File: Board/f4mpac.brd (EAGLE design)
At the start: 60.3 x 83.2 mm, 52 parts, among them CN1 DIP40 MB CONN, IC1 YM2413, IC10 27C512AL, IC2 74LS30D, IC3 74LS04D, IC4 LM4558N, IC5 Z80, IC6 74LS30D, IC7 74LS02D, IC8 74LS74D, IC9 74LS125D

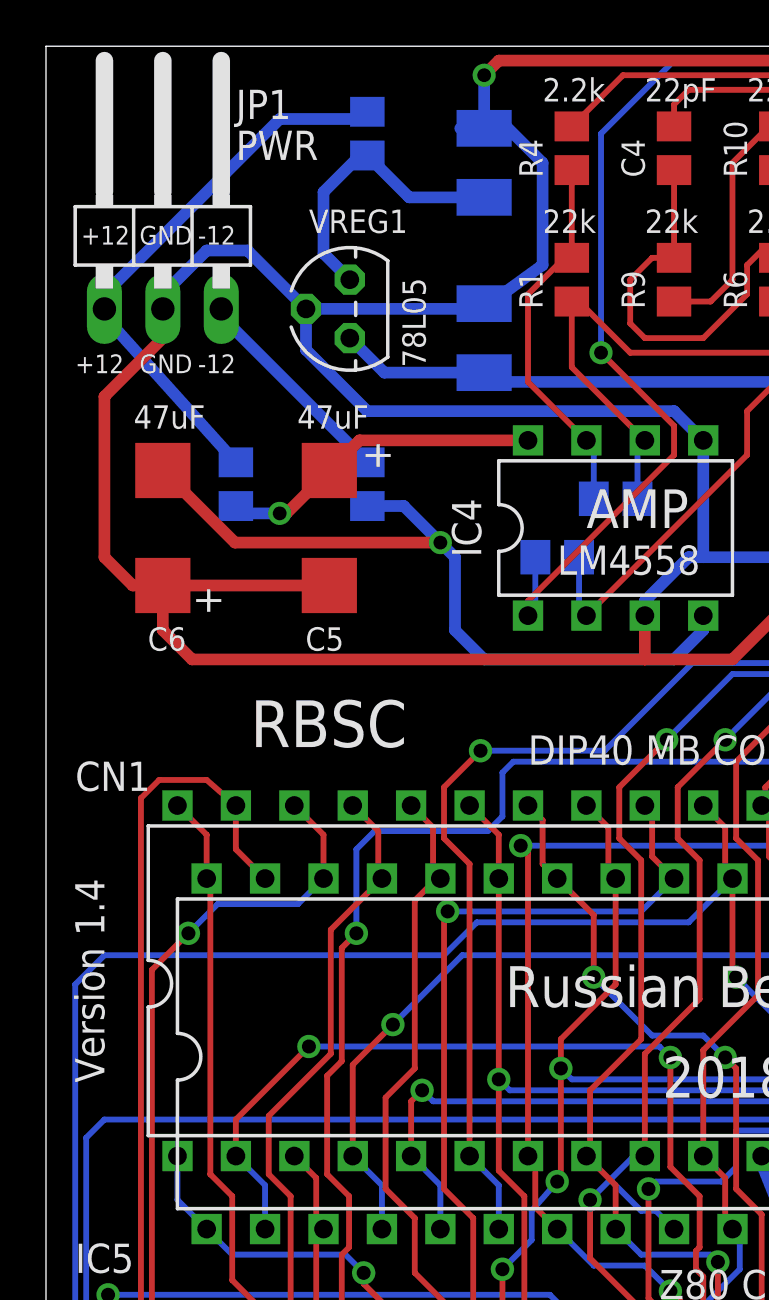
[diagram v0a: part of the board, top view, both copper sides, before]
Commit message: Updated 14.05.2025
Updated the board to version 1.5. Corrected R4, C14 and C16 values. Updated readme file.
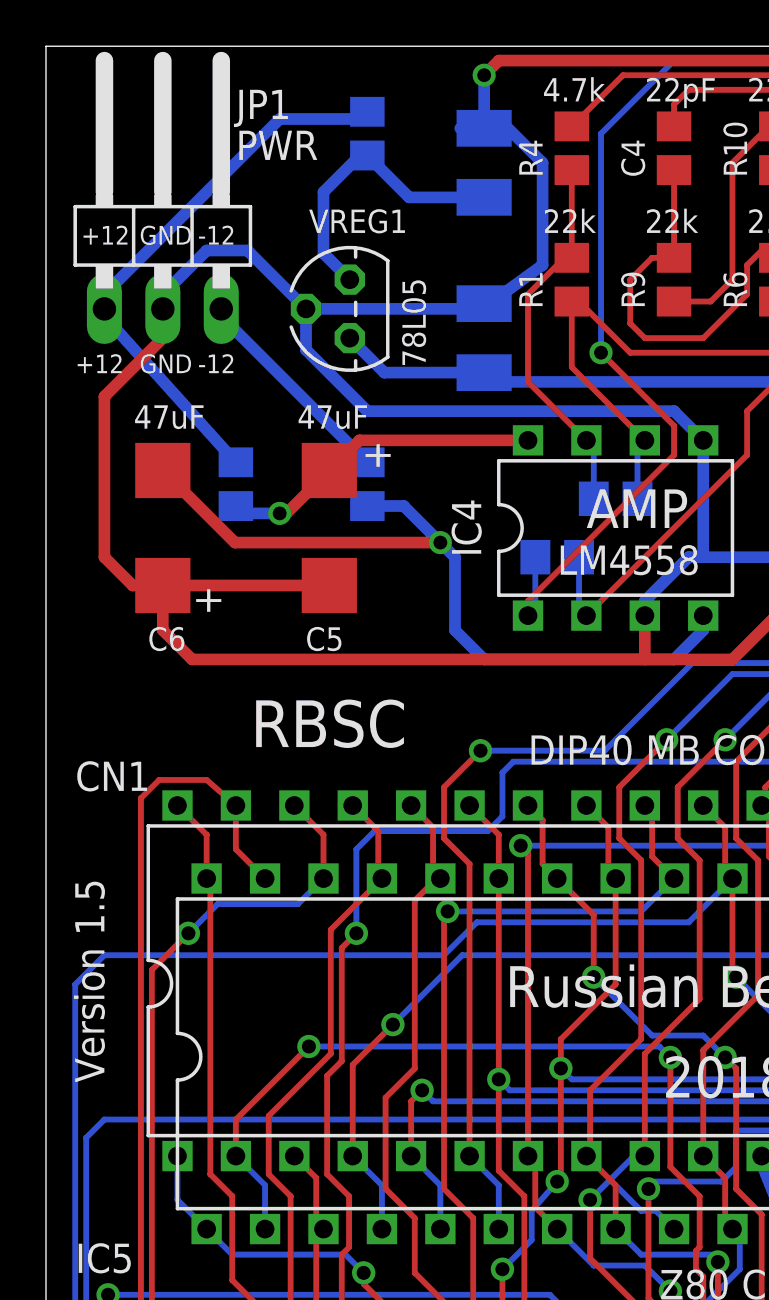
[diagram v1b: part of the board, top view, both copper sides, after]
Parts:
- C14, C16: value 1nF -> 470pF
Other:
- board text added: "470pF"
- board text added: "Version 1.5"
- board text removed: "1nF"
- board text removed: "Version 1.4"
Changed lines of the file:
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@@
 <text x="21.59" y="74.422" size="1.016" layer="25" font="vector">22k</text>
 <text x="34.925" y="74.422" size="1.016" layer="25" font="vector">2.2k</text>
-<text x="21.59" y="80.137" size="1.016" layer="25" font="vector">2.2k</text>
+<text x="21.59" y="80.137" size="1.016" layer="25" font="vector">4.7k</text>
 <text x="43.815" y="74.422" size="1.016" layer="25" font="vector">2.2k</text>
 <text x="26.035" y="74.422" size="1.016" layer="25" font="vector">22k</text>
@@
 <wire x1="20.32" y1="3.81" x2="40.64" y2="3.81" width="0.254" layer="25"/>
 <wire x1="40.64" y1="3.81" x2="40.64" y2="25.4" width="0.254" layer="25"/>
-<text x="17.145" y="61.595" size="1.016" layer="26" font="vector" rot="MR180">C14</text>
-<text x="17.145" y="60.325" size="1.016" layer="26" font="vector" rot="MR180">1nF</text>
+<text x="17.145" y="60.96" size="1.016" layer="26" font="vector" rot="MR180">C14</text>
+<text x="17.145" y="62.23" size="1.016" layer="26" font="vector" rot="MR180">470pF</text>
 <text x="11.43" y="74.422" size="1.016" layer="25" font="vector">VREG1</text>
 <text x="16.51" y="68.58" size="1.016" layer="25" font="vector" rot="R90">78L05</text>
@@
 <wire x1="40.64" y1="25.4" x2="20.32" y2="25.4" width="0.254" layer="25"/>
 <wire x1="20.32" y1="25.4" x2="20.32" y2="3.81" width="0.254" layer="25"/>
-<text x="26.797" y="71.12" size="1.27" layer="26" font="vector" rot="MR180">Version 1.4</text>
-<text x="1.27" y="46.355" size="1.27" layer="25" font="vector" rot="R270">Version 1.4</text>
+<text x="26.797" y="71.12" size="1.27" layer="26" font="vector" rot="MR180">Version 1.5</text>
+<text x="1.27" y="46.355" size="1.27" layer="25" font="vector" rot="R270">Version 1.5</text>
 <text x="34.29" y="15.24" size="1.27" layer="25" font="vector" rot="R180">27c256</text>
 <text x="54.737" y="15.24" size="1.27" layer="25" font="vector">JP4</text>
@@
 <text x="41.91" y="59.436" size="1.016" layer="26" font="vector" rot="MR0">100nF</text>
 <text x="60.071" y="14.732" size="1.27" layer="25" font="vector" rot="R180">ROMSEL</text>
-<text x="29.845" y="62.865" size="1.016" layer="26" font="vector" rot="MR0">C16</text>
-<text x="29.845" y="61.595" size="1.016" layer="26" font="vector" rot="MR0">1nF</text>
+<text x="29.845" y="62.23" size="1.016" layer="26" font="vector" rot="MR0">C16</text>
+<text x="29.845" y="60.96" size="1.016" layer="26" font="vector" rot="MR0">470pF</text>
 <text x="23.495" y="61.595" size="1.6764" layer="25" font="vector">AMP</text>
 <text x="43.18" y="61.595" size="1.6764" layer="25" font="vector">OPLL</text>
@@
 <element name="R12" library="rcl" package="R0805" value="100" x="8.255" y="63.5" smashed="yes" rot="MR90"/>
 <element name="JP2" library="pinhead" package="1X02/90" value="OE/CE" x="4.064" y="6.985" smashed="yes" rot="R180"/>
-<element name="C14" library="rcl" package="C0805" value="1nF" x="22.225" y="60.325" smashed="yes" rot="MR0"/>
+<element name="C14" library="rcl" package="C0805" value="470pF" x="22.225" y="60.325" smashed="yes" rot="MR0"/>
 <element name="C8" library="rcl" package="C0805" value="100nF" x="40.005" y="61.595" smashed="yes" rot="MR180"/>
-<element name="C16" library="rcl" package="C0805" value="1nF" x="24.765" y="62.865" smashed="yes" rot="MR0"/>
+<element name="C16" library="rcl" package="C0805" value="470pF" x="24.765" y="62.865" smashed="yes" rot="MR0"/>
 <element name="IC10" library="microchip" package="PLCC-32" value="27C512AL" x="30.48" y="15.24" smashed="yes" rot="R90">
 <attribute name="MPN" value="M27C512-90C1" x="30.48" y="15.24" size="1.778" layer="27" rot="R90" display="off"/>
